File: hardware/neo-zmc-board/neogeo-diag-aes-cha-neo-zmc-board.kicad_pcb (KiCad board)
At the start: 2 copper layers, 173 x 134 mm, 16 parts, among them J1 neogeo-aes-cha-a-side-edge, J2 neogeo-aes-cha-a-side-edge, J3 neogeo-aes-cha-b-side-edge, J4 neogeo-aes-cha-b-side-edge, U1 74HC574, U2 NEO-ZMC, U3 74HC574, U4 27C010 / 27C1001, U5 27C010 / 27C1001

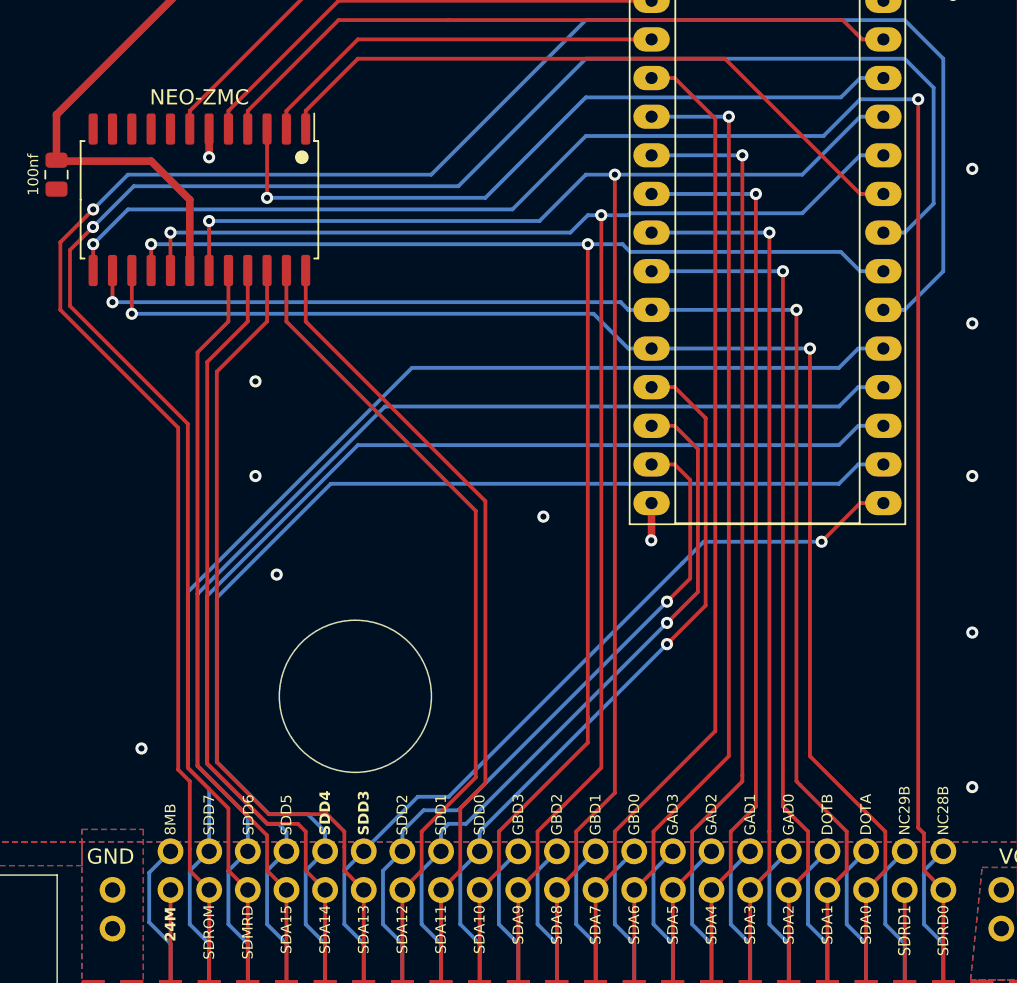
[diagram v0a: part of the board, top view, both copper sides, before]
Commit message: Minor tweaks, Bump revision number on all boards so they are the same
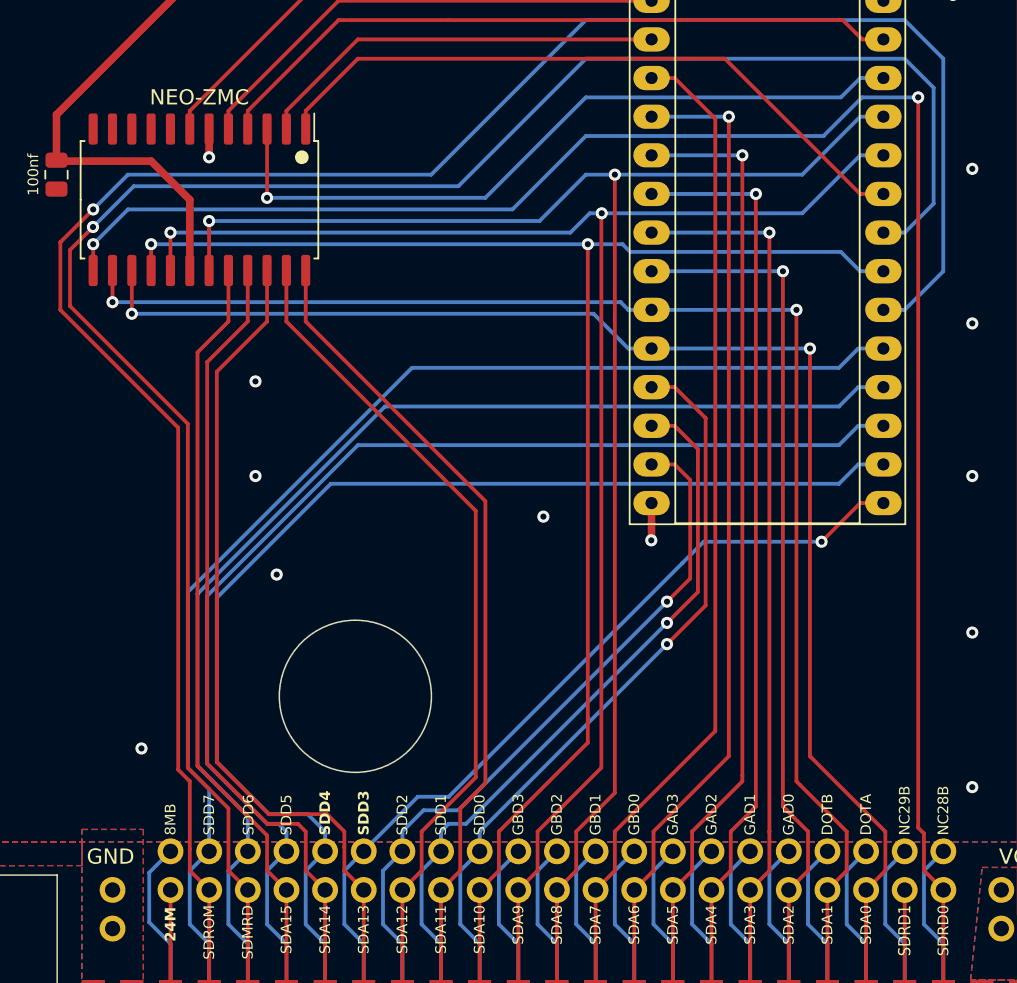
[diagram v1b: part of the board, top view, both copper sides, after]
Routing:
- net SDRD0: track 123.0 -> 123.7 mm
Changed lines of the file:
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@@
     )
   )
-  (property "REV" "2023-07-30")
+  (property "REV" "2023-08-20")
   (net 0 "")
   (net 1 "VCC")
@@
   (segment (start 156.85 141.38) (end 156.85 152.3) (width 0.25) (layer "F.Cu") (net 23))
   (segment (start 90.805 98.933) (end 90.805 100.662) (width 0.25) (layer "F.Cu") (net 24))
-  (segment (start 145.415 138.43) (end 145.415 137.668) (width 0.25) (layer "F.Cu") (net 24))
-  (segment (start 146.69 141.38) (end 146.69 152.3) (width 0.25) (layer "F.Cu") (net 24))
-  (segment (start 145.415 140.105) (end 145.415 138.43) (width 0.25) (layer "F.Cu") (net 24))
-  (segment (start 145.0345 137.2875) (end 145.0345 89.916) (width 0.25) (layer "F.Cu") (net 24))
+  (segment (start 145.0345 137.2875) (end 145.0345 89.2815) (width 0.25) (layer "F.Cu") (net 24))
   (segment (start 145.415 137.668) (end 145.0345 137.2875) (width 0.25) (layer "F.Cu") (net 24))
   (segment (start 146.69 141.38) (end 145.415 140.105) (width 0.25) (layer "F.Cu") (net 24))
+  (segment (start 145.415 140.105) (end 145.415 137.668) (width 0.25) (layer "F.Cu") (net 24))
+  (segment (start 146.69 141.38) (end 146.69 152.3) (width 0.25) (layer "F.Cu") (net 24))
+  (segment (start 145.0345 89.2815) (end 145.034 89.281) (width 0.25) (layer "F.Cu") (net 24))
   (via (at 90.805 98.933) (size 0.8) (drill 0.4) (layers "F.Cu" "B.Cu") (net 24))
-  (via (at 145.0345 89.408) (size 0.8) (drill 0.4) (layers "F.Cu" "B.Cu") (net 24))
-  (segment (start 123.1905 91.821) (end 138.8115 91.821) (width 0.25) (layer "B.Cu") (net 24))
-  (segment (start 93.091 96.647) (end 118.3645 96.647) (width 0.25) (layer "B.Cu") (net 24))
-  (segment (start 141.2245 89.408) (end 145.0345 89.408) (width 0.25) (layer "B.Cu") (net 24))
-  (segment (start 138.8115 91.821) (end 141.2245 89.408) (width 0.25) (layer "B.Cu") (net 24))
-  (segment (start 90.805 98.933) (end 93.091 96.647) (width 0.25) (layer "B.Cu") (net 24))
-  (segment (start 118.3645 96.647) (end 123.1905 91.821) (width 0.25) (layer "B.Cu") (net 24))
+  (via (at 145.034 89.281) (size 0.8) (drill 0.4) (layers "F.Cu" "B.Cu") (net 24))
+  (segment (start 138.8115 91.821) (end 123.1905 91.821) (width 0.25) (layer "B.Cu") (net 24))
+  (segment (start 118.3645 96.647) (end 93.091 96.647) (width 0.25) (layer "B.Cu") (net 24))
+  (segment (start 93.091 96.647) (end 90.805 98.933) (width 0.25) (layer "B.Cu") (net 24))
+  (segment (start 145.034 89.281) (end 141.3515 89.281) (width 0.25) (layer "B.Cu") (net 24))
+  (segment (start 141.3515 89.281) (end 138.8115 91.821) (width 0.25) (layer "B.Cu") (net 24))
+  (segment (start 123.1905 91.821) (end 118.3645 96.647) (width 0.25) (layer "B.Cu") (net 24))
   (segment (start 141.61 141.38) (end 141.61 152.3) (width 0.25) (layer "F.Cu") (net 25))
   (segment (start 137.9855 132.6515) (end 142.875 137.541) (width 0.25) (layer "F.Cu") (net 25))
@@
   (segment (start 120.1425 97.409) (end 123.1905 94.361) (width 0.25) (layer "B.Cu") (net 33))
   (segment (start 95.885 100.662) (end 95.885 98.171) (width 0.25) (layer "F.Cu") (net 34))
-  (segment (start 120.015 137.541) (end 124.2065 133.3495) (width 0.25) (layer "F.Cu") (net 34))
-  (segment (start 118.75 141.38) (end 120.015 140.115) (width 0.25) (layer "F.Cu") (net 34))
-  (segment (start 124.2065 133.3495) (end 124.2065 97.028) (width 0.25) (layer "F.Cu") (net 34))
-  (segment (start 120.015 140.115) (end 120.015 137.541) (width 0.25) (layer "F.Cu") (net 34))
+  (segment (start 124.2065 133.3495) (end 120.015 137.541) (width 0.25) (layer "F.Cu") (net 34))
+  (segment (start 124.2314 96.901) (end 124.2065 96.9259) (width 0.25) (layer "F.Cu") (net 34))
+  (segment (start 120.015 137.541) (end 120.015 140.115) (width 0.25) (layer "F.Cu") (net 34))
+  (segment (start 120.015 140.115) (end 118.75 141.38) (width 0.25) (layer "F.Cu") (net 34))
+  (segment (start 124.2065 96.9259) (end 124.2065 133.3495) (width 0.25) (layer "F.Cu") (net 34))
   (segment (start 118.75 141.38) (end 118.75 152.3) (width 0.25) (layer "F.Cu") (net 34))
-  (via (at 124.2065 97.028) (size 0.8) (drill 0.4) (layers "F.Cu" "B.Cu") (net 34))
+  (via (at 124.2314 96.901) (size 0.8) (drill 0.4) (layers "F.Cu" "B.Cu") (net 34))
   (via (at 95.885 98.171) (size 0.8) (drill 0.4) (layers "F.Cu" "B.Cu") (net 34))
-  (segment (start 122.1745 98.171) (end 123.3175 97.028) (width 0.25) (layer "B.Cu") (net 34))
-  (segment (start 123.3175 97.028) (end 124.2065 97.028) (width 0.25) (layer "B.Cu") (net 34))
+  (segment (start 123.4445 96.901) (end 122.1745 98.171) (width 0.25) (layer "B.Cu") (net 34))
+  (segment (start 124.2314 96.901) (end 123.4445 96.901) (width 0.25) (layer "B.Cu") (net 34))
   (segment (start 137.4145 96.901) (end 141.2255 93.09) (width 0.25) (layer "B.Cu") (net 34))
-  (segment (start 95.885 98.171) (end 122.1745 98.171) (width 0.25) (layer "B.Cu") (net 34))
-  (segment (start 124.2065 97.028) (end 125.9845 97.028) (width 0.25) (layer "B.Cu") (net 34))
+  (segment (start 122.1745 98.171) (end 95.885 98.171) (width 0.25) (layer "B.Cu") (net 34))
   (segment (start 141.2255 93.09) (end 142.7485 93.09) (width 0.25) (layer "B.Cu") (net 34))
-  (segment (start 126.1115 96.901) (end 137.4145 96.901) (width 0.25) (layer "B.Cu") (net 34))
-  (segment (start 125.9845 97.028) (end 126.1115 96.901) (width 0.25) (layer "B.Cu") (net 34))
+  (segment (start 124.2314 96.901) (end 137.4145 96.901) (width 0.25) (layer "B.Cu") (net 34))
   (segment (start 123.3175 131.6985) (end 123.3175 130.048) (width 0.25) (layer "F.Cu") (net 35))
   (segment (start 116.21 141.38) (end 117.475 140.115) (width 0.25) (layer "F.Cu") (net 35))
